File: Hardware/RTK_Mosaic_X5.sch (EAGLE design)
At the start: 187 parts, among them J2 MAGJACK-POE, J3 MICRO-SD-PUSH-PUSH-EXT-PIN, J4 Vertical Qwiic Connector, J9 MAGJACK-POE, U1 ESP32-WROVER-IE, U10 POE_PSU-DP990X, U17 URB2405YMD, U2 CH340C, U3 XC6222B331MR-G, U4 TXS0108, U5 TXS0108, U6 XC6222B331MR-G

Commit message: Ready for airwire review
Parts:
- removed C12, C37: 0.1uF, SparkFun-Capacitors:0.1UF-0603-25V-5%
- removed D2: LED-RIGHT-ANGLE-PTH-GREEN, SparkFun-LED:LED-RIGHT-ANGLE-PTH-GREEN
- removed LED: JUMPER-SMT_2_NC_TRACE_SILK, SparkFun-Jumpers:JUMPER-SMT_2_NC_TRACE_SILK
- removed R62: 470, SparkFun-Resistors:470OHM-0603-1/10W-1%
- removed TP_LED: TEST-POINTPOGO_PTH, SparkFun-Connectors:TEST-POINTPOGO_PTH
- removed U$108: KSZ8041NL, Septentrio_Mosaic:KSZ8041NL
- removed U$2: MOSAIC-X5X5, Septentrio_Mosaic:MOSAIC-X5X5
- added 2V8, COM2_CTS, COM2_RTS, COM2_RX, COM2_TX, COM3_CTS, COM3_RTS, COM3_RX, COM3_TX, GPIO_1, GPIO_2, RDY, REF: TEST-POINTPOGO_PTH, SparkFun-Connectors:TEST-POINTPOGO_PTH
- added BT, LOG, PVT, RTK, WIFI: JUMPER-SMT_2_NC_TRACE_SILK, SparkFun-Jumpers:JUMPER-SMT_2_NC_TRACE_SILK
- added C60, C61: 2.2uF, SparkFun-Capacitors:2.2UF-0603-10V-20%
- added C62: 0.1uF, SparkFun-Capacitors:0.1UF-0603-25V-5%
- added D11: LED-RIGHT-ANGLE-PTH-AMBER, SparkFun-LED:LED-RIGHT-ANGLE-PTH-AMBER
- added D12, D15, D16: LED-RIGHT-ANGLE-PTH-BLUE, SparkFun-LED:LED-RIGHT-ANGLE-PTH-BLUE
- added D13: LED-RIGHT-ANGLE-PTH-GREEN, SparkFun-LED:LED-RIGHT-ANGLE-PTH-GREEN
- added D17: PESD0402, SparkFun-DiscreteSemi:PESD0402-0402
- added FB3: 470Ω, SparkFun-Coils:FERRITE_BEAD-0603-470Ω-100MHZ-1A-200MILIΩ
- added LOG_BTN: MOMENTARY-SWITCH-SPST-PTH-RIGHT-ANGLE-8-020, SparkFun-Switches:MOMENTARY-SWITCH-SPST-PTH-RIGHT-ANGLE-8-020
- added MOSAIC_RF: ANTENNA-SMA-GROUNDEDEDGE_SMA, SparkFun-RF:ANTENNA-SMA-GROUNDEDEDGE_SMA
- added R18, R22, R23, R43, R44: 10k, SparkFun-Resistors:10KOHM-0603-1/10W-1%
- added R20, R21: 4.7k, SparkFun-Resistors:4.7KOHM-0603-1/10W-1%
- added R27, R28, R36, R37, R38, R39: 1k, SparkFun-Resistors:1KOHM-0603-1/10W-1%
- added U11: SN74AVC4T774PW, SparkFun-IC-Comms:SN74AVC4T774PW
- added U8: MOSAIC-X5X5, Septentrio_Mosaic:MOSAIC-X5X5
- added U9: KSZ8041NL, Septentrio_Mosaic:KSZ8041NL
- renumbered GNSS_RESET to MOSAIC_RST, U$91 to U7
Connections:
- removed net ESP2/LED: R62.1, TP_LED.1
- removed net GNSS_!RESET!: MOSAIC_RST.1
- removed net N$45: D2.A, LED.1
- removed net N$7: LED.2, R62.2
- removed net SD_DAT0: J3.DAT0/SDO
- new net 1.8V: C60.1, C62.1, R18.2, U11.A4, U11.DIR3, U11.DIR4, U11.VCCA, U8.1V8_OUT
- new net 2V8: 2V8.1, U8.2V8_IN, U8.2V8_OUT
- new net COM2_CTS: COM2_CTS.1, U8.COM2_CTS
- new net COM2_RTS: COM2_RTS.1, U8.COM2_RTS
- new net COM2_RX: COM2_RX.1, U8.COM2_RX
- new net COM2_TX: COM2_TX.1, U8.COM2_TX
- new net COM3_CTS: COM3_CTS.1, U8.COM3_CTS
- new net COM3_RTS: COM3_RTS.1, U8.COM3_RTS
- new net COM3_RX: COM3_RX.1, U8.COM3_RX
- new net COM3_TX: COM3_TX.1, U8.COM3_TX
- new net GPIO_1: GPIO_1.1, U8.GPIO_1
- new net GPIO_2: GPIO_2.1, U8.GPIO_2
- new net LED_PVT: R38.1, U8.GP_LED
- new net LED_RTK: R39.1, U8.GP_LED2
- new net LOG_LED: R37.1, U8.LOG_LED
- new net MOSAIC_!RST!: MOSAIC_RST.1, U8.!RST!
- new net MOSAIC_EVENTA_1V8: U11.A1, U8.EVENTA
- new net MOSAIC_EVENTB_1V8: U11.A2, U8.EVENTB
- new net MOSAIC_PPSO_1V8: U11.A3, U8.PPS
- new net MOSAIC_RF: D17.1, MOSAIC_RF.SIGNAL, U8.ANT_1
- new net N$11: LOG_BTN.2, R27.1
- new net N$16: LOG.2, R37.2
- new net N$17: D13.A, LOG.1
- new net N$18: D11.A, WIFI.1
- new net N$22: BT.1, D12.A
- new net N$26: BT.2, R36.2
- new net N$32: R28.2, WIFI.2
- new net N$35: D15.A, PVT.1
- new net N$36: D16.A, RTK.1
- new net N$37: R39.2, RTK.2
- new net N$38: PVT.2, R38.2
- new net N$6: FB3.2, U8.VANT
- new net N$9: R18.1, U8.SYNC
- new net RDY: RDY.1, U8.MODULE_RDY
- new net REF: REF.1, U8.REF_IN, U8.REF_OUT
- net 3.3V: now also R21.2
- net 3.3V_SW: now also R20.2, U11.VCCB, U8.VDD_3V3, U8.VDD_BAT, U9.VDDIO; no longer U$108.VDDIO, U$2.VDD_3V3, U$2.VDD_BAT
- net 5V: now also C61.1, FB3.1, U8.V_USB; no longer U$2.VANT, U$2.V_USB
- net ACT_MOSAIC: now also U9.LED1/SPEED; no longer U$108.LED1/SPEED
- net D+_MOSAIC: now also U8.USB_D+; no longer U$2.USB_D+
- net D-_MOSAIC: now also U8.USB_D-; no longer U$2.USB_D-
- net ESP12_LED_WIFI: now also R28.1
- net ESP15_LED_BT: now also R36.1
- net ESP18_MDIO: now also R21.1
- net ESP2_COM4_RX: now also U8.COM4_RX; no longer U$2.COM4_RX
- net ESP32_TX: now also U5.A2; no longer U5.A1
- net ESP32_TX_IO: now also U5.B2; no longer U5.B1
- net ESP33_RTS: now also U5.A3; no longer U5.A2
- net ESP33_RTS_IO: now also U5.B3; no longer U5.B2
- net ESP34_RX: now also U5.A1; no longer U5.A3
- net ESP34_RX_IO: now also U5.B1; no longer U5.B3
- net ESP4_COM4_TX: now also U8.COM4_TX; no longer U$2.COM4_TX
- net ETHER_!RST!: now also R22.2, U8.ETHER_!RST!, U9.!RST!; no longer U$2.ETHER_!RST!
- net ETHER_CLK: now also U8.ETHER_CLK, U9.XI/REFCLK; no longer U$108.XI/REFCLK, U$2.ETHER_CLK
- net ETHER_CRSDV: now also U8.ETHER_CRSDV, U9.RXDV/CONFIG2; no longer U$108.RXDV/CONFIG2, U$2.ETHER_CRSDV
- net ETHER_MDC: now also U8.ETHER_MDC, U9.MDC; no longer U$108.MDC, U$2.ETHER_MDC
- net ETHER_MDIO: now also R20.1, U8.ETHER_MDIO, U9.MDIO; no longer U$108.MDIO, U$2.ETHER_MDIO
- net ETHER_RXD0: now also U8.ETHER_RXD0, U9.RXD0/DUPLEX; no longer U$108.RXD0/DUPLEX, U$2.ETHER_RXD0
- net ETHER_RXD1: now also U8.ETHER_RXD1, U9.RXD1/PHYAD2; no longer U$108.RXD1/PHYAD2, U$2.ETHER_RXD1
- net ETHER_RXER: now also U8.ETHER_RXER, U9.RXER/ISO; no longer U$108.RXER/ISO, U$2.ETHER_RXER
- net ETHER_TXD0: now also U8.ETHER_TXD0, U9.TXD0; no longer U$108.TXD0, U$2.ETHER_TXD0
- net ETHER_TXD1: now also U8.ETHER_TXD1, U9.TXD1; no longer U$108.TXD1, U$2.ETHER_TXD1
- net ETHER_TXEN: now also U8.ETHER_TXEN, U9.TXEN; no longer U$108.TXEN, U$2.ETHER_TXEN
- net GND: now also C60.2, C61.2, C62.2, D11.C, D12.C, D13.C, D15.C, D16.C, D17.2, LOG_BTN.1, MOSAIC_RF.GND, R22.1, R43.1, R44.1, U11.!OE, U11.DIR1, U11.DIR2, U11.GND, U8.ANT_2, U8.GND, U8.RTC_XTALI, U9.GND; no longer C12.2, C37.2, D2.C, U$108.GND
- net LINK_MOSAIC: now also U9.LED0/NWAYEN; no longer U$108.LED0/NWAYEN
- net MOSAIC_CTS: now also U8.COM1_CTS; no longer U$2.COM1_CTS
- net MOSAIC_EVENTA: now also U11.B1; no longer U$2.EVENTA
- net MOSAIC_EVENTA_IO: now also R43.2
- net MOSAIC_EVENTB: now also U11.B2; no longer U$2.EVENTB
- net MOSAIC_EVENTB_IO: now also R44.2
- net MOSAIC_LOG_BTN: now also U8.LOG_BTN; no longer U$2.LOG_BTN
- net MOSAIC_LOG_BTN_IO: now also R23.2, R27.2
- net MOSAIC_PPSO: now also U11.B3; no longer U$2.PPS
- net MOSAIC_RTS: now also U8.COM1_RTS; no longer U$2.COM1_RTS
- net MOSAIC_RX: now also U8.COM1_RX; no longer U$2.COM1_RX
- net MOSAIC_TX: now also U8.COM1_TX; no longer U$2.COM1_TX
- net N$146: now also U9.VDDP; no longer U$108.VDDP
- net N$147: now also U9.REXT; no longer U$108.REXT
- net N$148: now also U9.COL/CONFIG0; no longer U$108.COL/CONFIG0
- net RD+_MOSAIC: now also D1.IO1, U9.RX+; no longer D1.IO3, U$108.RX+
- net RD-_ESP32: now also D7.IO4; no longer D7.IO2
- net RD-_MOSAIC: now also U9.RX-; no longer U$108.RX-
- net SD_CLK: now also U8.SD_CLK; no longer U$2.SD_CLK
- net SD_CMD: now also U8.SD_CMD; no longer U$2.SD_CMD
- net SD_DATA: now also J3.DAT0/SDO, U8.SD_DATA; no longer U$2.SD_DATA
- net TD+_ESP32: now also D7.IO2; no longer D7.IO4
- net TD+_MOSAIC: now also U9.TX+; no longer U$108.TX+
- net TD-_MOSAIC: now also D1.IO3, U9.TX-; no longer D1.IO1, U$108.TX-
- net VCCA: no longer C37.1
- net VCCIO: now also R23.1
- net VDDA: now also U9.VDDA; no longer C12.1, U$108.VDDA
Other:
- note added: "LEDs"
- note added: "Log / Unmount SD Button"
- note added: "No clean process"
- note removed: "LED"
- moved on the sheet: ACT2, BOOT, BOOT_SW, C11, C13, C23, C24, C25, C26, C29, C30, C33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

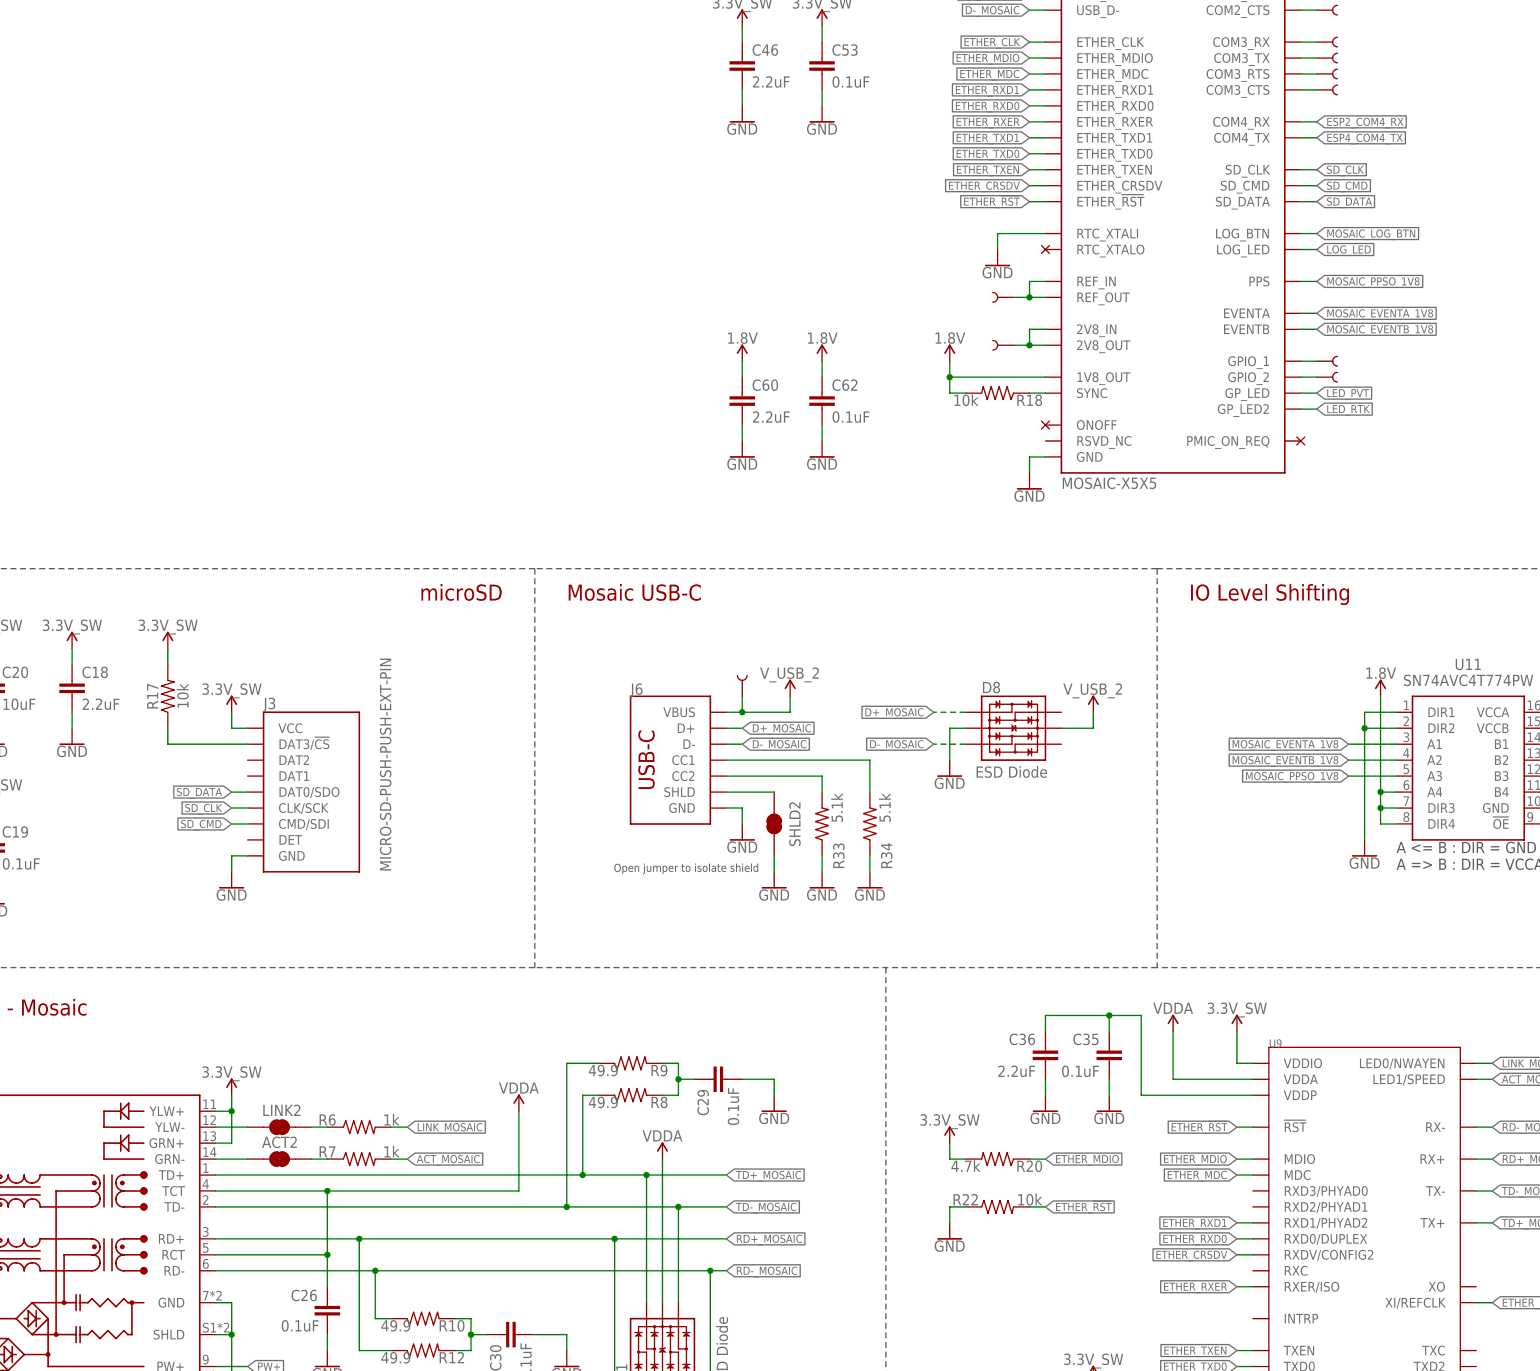
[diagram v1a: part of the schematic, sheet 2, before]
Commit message: Silk added. Layer 15 polygon is now GND.
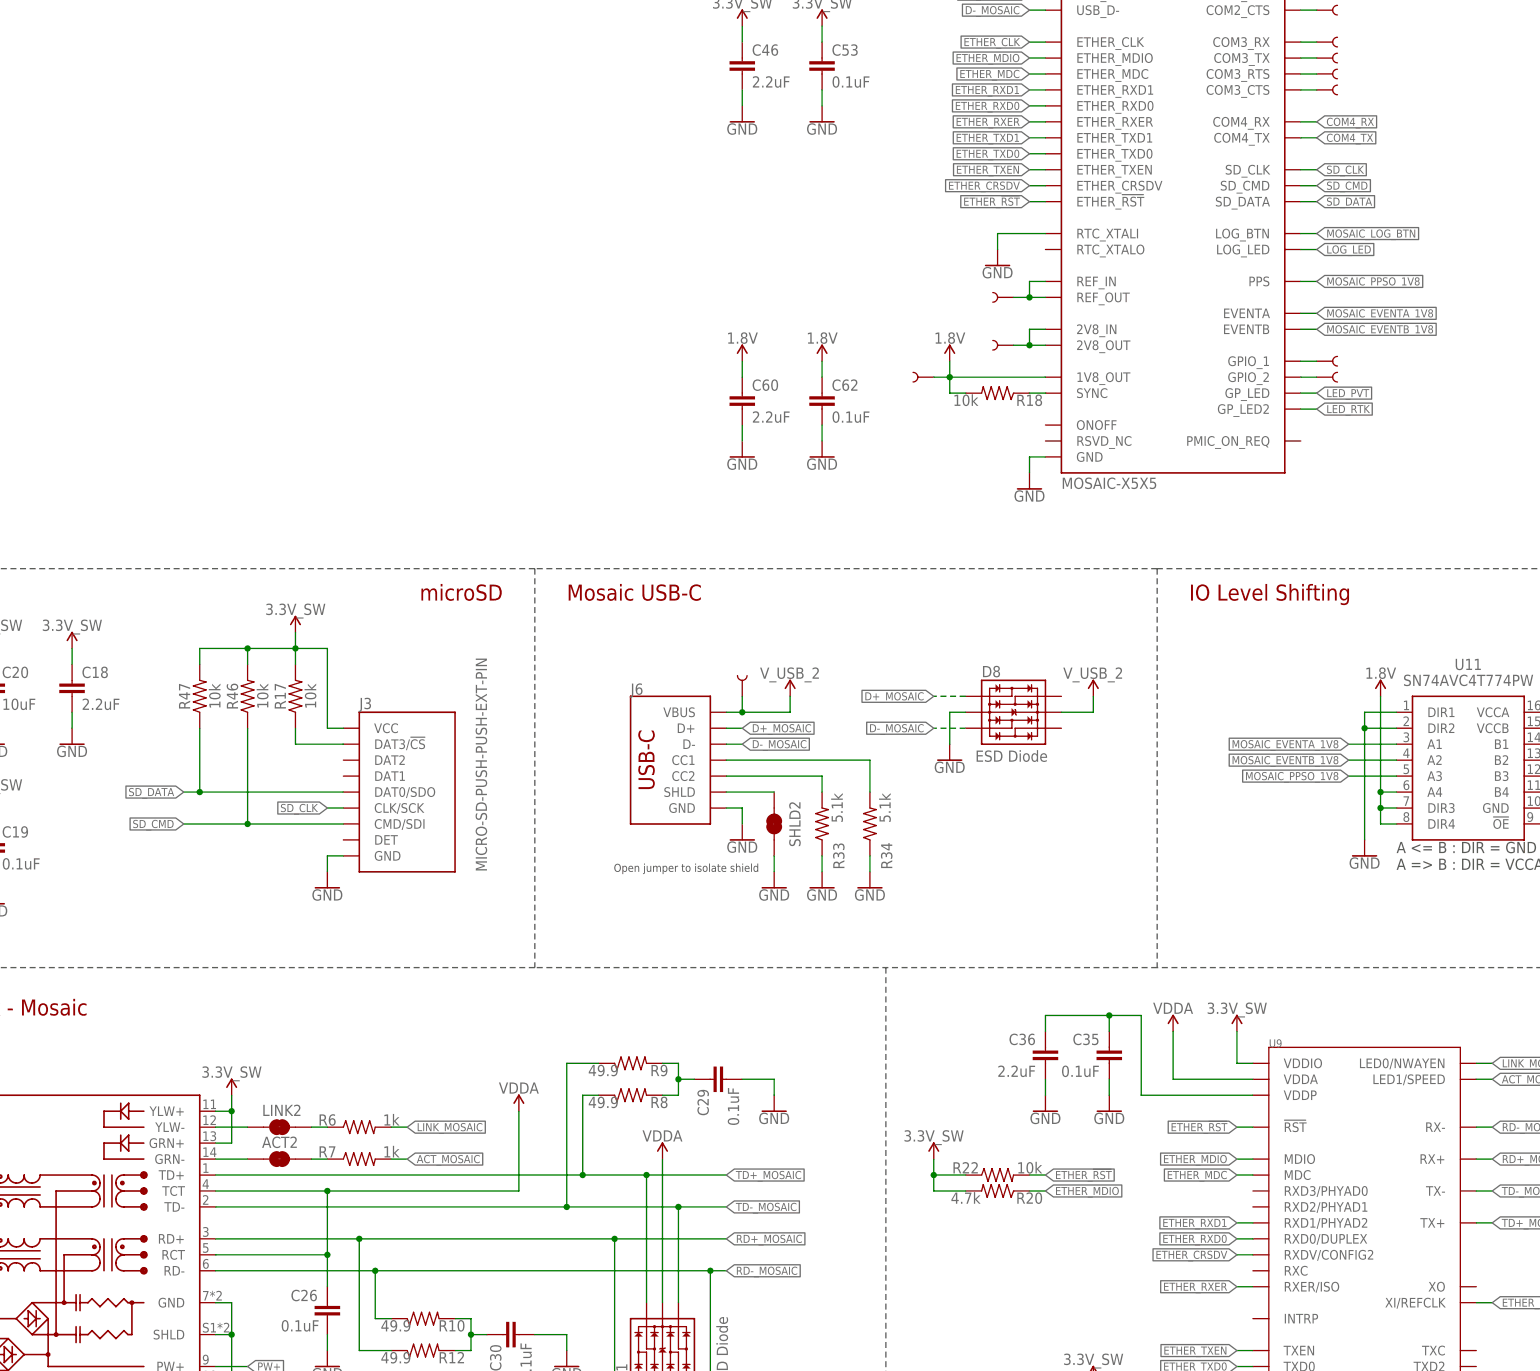
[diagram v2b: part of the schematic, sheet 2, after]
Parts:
- added 1V8: TEST-POINTPOGO_PTH, SparkFun-Connectors:TEST-POINTPOGO_PTH
- added R46, R47, R48, R49, R50: 10k, SparkFun-Resistors:10KOHM-0603-1/10W-1%
- added R51, R52: 0, SparkFun-Resistors:0OHM-0603-1/10W
- added R_SCL, R_SDA: 2.2k, SparkFun-Resistors:2.2KOHM-0603-1/10W-1%
- R16: value 2.2k -> 10k; device SparkFun-Resistors:2.2KOHM-0603-1/10W-1% -> SparkFun-Resistors:10KOHM-0603-1/10W-1%
- R19: value 2.2k -> 1k; device SparkFun-Resistors:2.2KOHM-0603-1/10W-1% -> SparkFun-Resistors:1KOHM-0603-1/10W-1%
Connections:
- net N$3 renamed SD_DAT3
- removed net ESP0/!BOOT!: BOOT_SW.1, Q1G2.C, TP_BOOT.1, U1.IOA0, U7.XI/REFCLK
- removed net ESP2_COM4_RX: U1.IOA2, U8.COM4_RX
- removed net ESP4_COM4_TX: U1.IOA4, U8.COM4_TX
- new net !BOOT!: BOOT_SW.1, Q1G2.C, R16.1, R19.2, TP_BOOT.1
- new net COM4_RX: R52.2, U8.COM4_RX
- new net COM4_TX: R51.2, U8.COM4_TX
- new net ESP2_TX: R48.1, R52.1, U1.IOA2
- new net ESP4_RX: R51.1, U1.IOA4
- new net ESP_REFCLK: R19.1, U1.IOA0, U7.XI/REFCLK
- net 1.8V: now also 1V8.1
- net 3.3V: now also R16.2, R49.2
- net 3.3V_SW: now also R22.1, R46.2, R47.2
- net ESP12_LED_WIFI: now also R50.1
- net ESP14_SCL: now also R_SCL.1; no longer R16.1
- net ESP15_SDA: now also R_SDA.1; no longer R19.1
- net ESP5_ERST: now also R49.1
- net GND: now also R48.2, R50.2; no longer R22.1
- net N$14: now also R_SCL.2; no longer R16.2
- net N$15: now also R_SDA.2; no longer R19.2
- net SD_CMD: now also R46.1
- net SD_DATA: now also R47.1
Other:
- note added: "IO0: Avoid device connections."
- note added: "IO15: Has builtin pullup at POR. Also pulled up by R_SDA."
- note removed: "IO0: Avoid device connections. Can be used a stat LED."
- note removed: "IO15: Has builtin pullup at POR."
- moved on the sheet: D3, D8, ESP32_RF, J3, J8, R16, R17, R19, R20, R22
